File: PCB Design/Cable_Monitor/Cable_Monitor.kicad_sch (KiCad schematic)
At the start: 13 parts, among them P1 ${SIM.PARAMS}, P2 ${SIM.PARAMS}

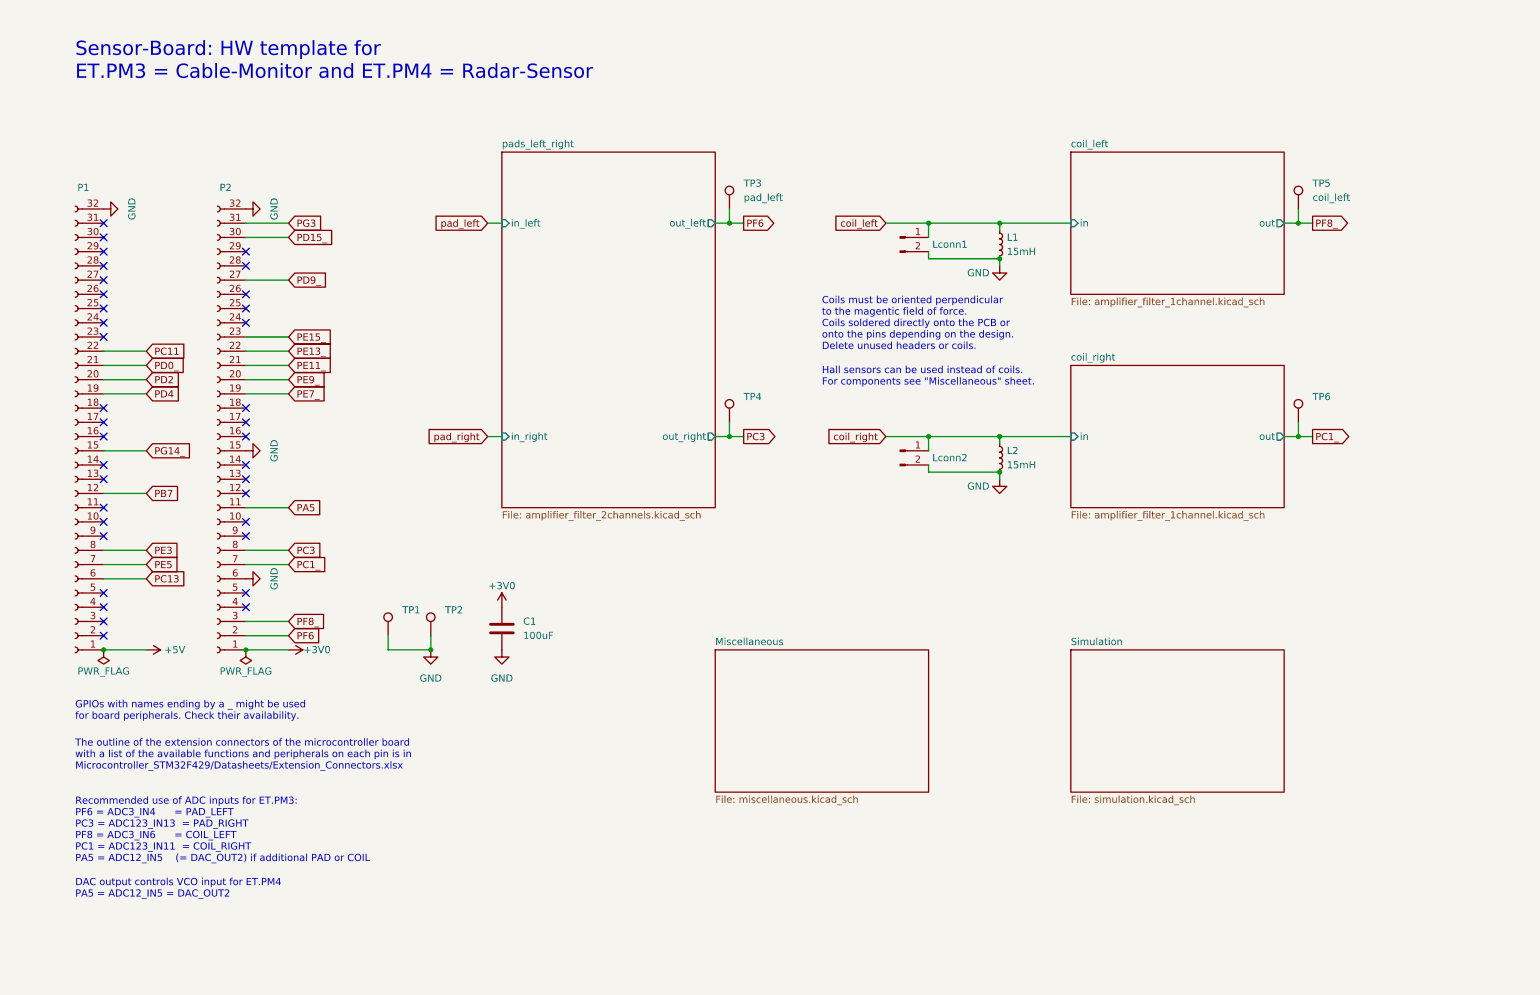
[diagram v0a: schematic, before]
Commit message: Modified Schematics
Added Virtual GND and adapted the Pads Left and Right
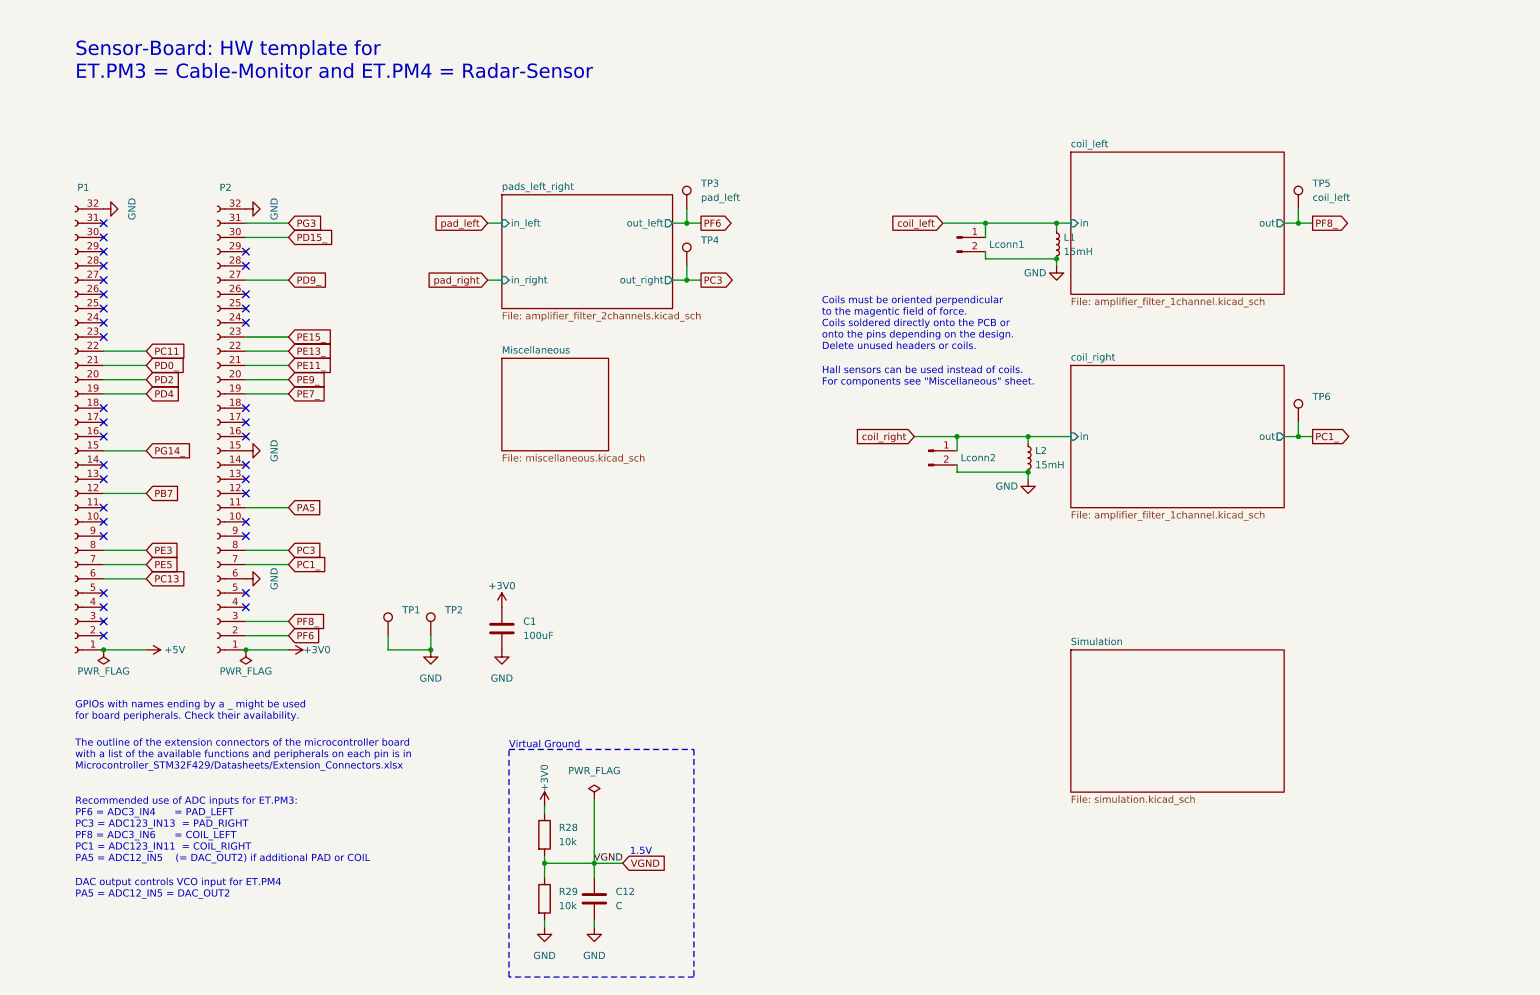
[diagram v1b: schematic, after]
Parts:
- added C12: C, symbol Device:C
- added R28, R29: 10k, symbol Device:R
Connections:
- net +3V0: now also R28.1
- net GND: now also C12.2, R29.2
- new net VGND: C12.1, R28.2, R29.1
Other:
- note added: "1.5V"
- note added: "Virtual Ground"
- moved on the sheet: L1, L2, Lconn1, Lconn2, TP3, TP4

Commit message: PCB Layout Update
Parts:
- added C4: 4.7uF, Capacitor_SMD:C_1206_3216Metric_Pad1.33x1.80mm_HandSolder, symbol Device:C
- added C4: C, symbol Device:C
- added C6: 100nF, Capacitor_SMD:C_0805_2012Metric_Pad1.18x1.45mm_HandSolder, symbol Device:C
- added C7: 10uF, Capacitor_SMD:C_0805_2012Metric_Pad1.18x1.45mm_HandSolder, symbol Device:C
- added J1: USB_B_Micro, symbol Connector:USB_B_Micro
- added TP3: Virtual Ground TP, symbol Connector:TestPoint
- added U3: SiP32508, Package_TO_SOT_SMD:TSOT-23-6_HandSoldering, symbol HW_template:SiP32508
- added U4: LD1117S33TR, Package_TO_SOT_SMD:SOT-223-3_TabPin2, symbol Regulator_Linear:LD1117S33TR_SOT223
- renumbered C12 to C2, L2 to L1, L1 to L2, Lconn2 to Lconn1, Lconn1 to Lconn2, R28 to R1, R29 to R2, TP3 to TP4, TP4 to TP5, TP5 to TP6, TP6 to TP7
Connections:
- net +3V0: now also C7.1, U4.2 (VO)
- net +5V: now also C4.1, C4.1, J1.1 (VBUS), U3.5 (IN), U3.6 (IN)
- net GND: now also C4.2, C4.2, C6.2, C7.2, J1.5 (GND), J1.6 (Shield), U3.4 (GND), U4.1 (GND)
- net VGND: now also TP3.1
- new net: C6.1, U3.1 (OUT), U3.2 (OUT), U4.3 (VI)
- new net Enable: U3.3 (EN)
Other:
- note added: "C4, C6 & C7 Values from Datasheet"
- note added: "Linear 3.3V low drop regulator"
- note added: "Load switch Can be used to power on with pushbutton and power off via microcontroller."
- note added: "Micro USB Connector for 5V external supply (Powerbank)"
- company: hhrt@zhaw.ch -> ZHAW
- title: Sensor-Board: HW template for ET.PM3 and ET.PM4 -> Cable Monitor
- moved on the sheet: C1, C2, R1, R2, TP1, TP2

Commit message: PCB Design Update
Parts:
- removed L1, L2: 15mH, Inductor_SMD:L_Bourns_SRN6045TA, symbol Device:L_Small
- removed Lconn1: Conn_01x02_Male, Connector_PinHeader_2.54mm:PinHeader_1x02_P2.54mm_Vertical, symbol Connector:Conn_01x02_Pin
- added BZ1: Buzzer, Buzzer_Beeper:Buzzer_12x9.5RM7.6, symbol Device:Buzzer
- added C? (x2): 100nF, Capacitor_SMD:C_0805_2012Metric_Pad1.18x1.45mm_HandSolder, symbol Device:C
- added LED1 (x2): LEDred_3mm, LED_THT:LED_D3.0mm, symbol Device:LED
- added Lconn2: Conn_01x02_Male, Connector_PinHeader_2.54mm:PinHeader_1x02_P2.54mm_Vertical, symbol Connector:Conn_01x02_Pin
- added Q1: BSS316N, Package_TO_SOT_SMD:SOT-23, symbol Transistor_FET:BSS138
- added R21 (x2): 62, Resistor_SMD:R_0805_2012Metric_Pad1.20x1.40mm_HandSolder, symbol Device:R
- added R26: 100k, Resistor_SMD:R_0805_2012Metric_Pad1.20x1.40mm_HandSolder, symbol Device:R
- added SW1: ${SIM.PARAMS}, Button_Switch_SMD:SW_SPST_PTS645, symbol Switch:SW_Push
- added U? (x2): DRV5053_THT, HW_template:TO-92Flat_wide, symbol Sensor_Magnetic:DRV5055A1xLPGxQ1
- C2: value C -> 1nF
- TP6: value coil_left -> HS_left
- TP7: value ${SIM.PARAMS} -> HS_right
- renumbered C4 to C?, C7 to C?, C6 to C?, Lconn2 to Lconn1, U4 to U?, U3 to U?
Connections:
- net +3V0: now also C?.2, C?.2, U?.1 (VCC), U?.1 (VCC)
- net +5V: now also BZ1.1 (-)
- net GND: now also C?.1, C?.1, LED1.1 (K), LED1.1 (K), Lconn2.2 (Pin_2), Q1.2 (S), R26.2, U?.2 (GND), U?.2 (GND)
- net PA5: now also Q1.1 (G), R26.1
- net coil_left renamed HS_left
- net HS_left: now also U?.3 (OUT)
- new net: BZ1.2 (+), Q1.3 (D)
- new net: LED1.2 (A), R21.2 (x2)
- new net HS_right: Lconn2.1 (Pin_1), U?.3 (OUT)
- new net LED_LEFT_EN: R21.1
- new net LED_RIGHT_EN: R21.1
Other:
- sheet coil_left renamed hall-sensor_left_right
- removed sheet Simulation
- removed sheet coil_right
- sheet hall-sensor_left_right ports: added in_left, in_right, out_left, out_right; removed in, out
- note added: "PWM controlled Buzzer"
- note removed: "Coils must be oriented perpendicular to the magentic field of force. Coils soldered directly onto the PCB or onto the pins depending on the design. Delete unused headers or coils."
- note removed: "Hall sensors can be used instead of coils. For components see "Miscellaneous" sheet."
- moved on the sheet: TP6, TP7

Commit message: Letzte Anpassungen am Schema
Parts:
- added TP14: PWM_Buzzer, TestPoint:TestPoint_Loop_D2.60mm_Drill1.6mm_Beaded, symbol Connector:TestPoint
- added TP3, TP4: pad_left_in, TestPoint:TestPoint_Loop_D2.60mm_Drill1.6mm_Beaded, symbol Connector:TestPoint
- added TP8: HS_left_in, TestPoint:TestPoint_Loop_D2.60mm_Drill1.6mm_Beaded, symbol Connector:TestPoint
- added TP9: HS_right_in, TestPoint:TestPoint_Loop_D2.60mm_Drill1.6mm_Beaded, symbol Connector:TestPoint
- C4: value C -> 100uF
- TP10: renamed from TP6; value HS_left -> HS_left_out
- TP11: renamed from TP7; value HS_right -> HS_right_out
- TP6: renamed from TP4; value pad_left -> pad_left_out
- TP7: renamed from TP5; value ${SIM.PARAMS} -> pad_right_out
- gave numbers to parts that had none: 9
- renumbered TP3 to TP5
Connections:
- net LED_LEFT_EN is gone; now on net PE15_: R21.1
- net LED_RIGHT_EN is gone; now on net PE13_: R21.1
- net PA5: now also TP14.1
- net pad_left: now also TP3.1
- net pad_right: now also TP4.1
- net HS_left renamed hall-sensor_left_right/in_left
- net hall-sensor_left_right/in_left: now also TP8.1
- net HS_right renamed hall-sensor_left_right/in_right
- net hall-sensor_left_right/in_right: now also TP9.1
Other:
- removed sheet Miscellaneous
- note added: "Cable-Monitor A Project by A.Horvat and T.Wey for PM3 Module ZHAW"
- note added: "Left and Right LED's to show direction of Fields"
- note added: "Pads for picking up Electrical Field. Including Filtering and amplifying"
- note removed: "Sensor-Board: HW template for ET.PM3 = Cable-Monitor and ET.PM4 = Radar-Sensor"
- moved on the sheet: BZ1, C1, LED1, Q1, R21, R26, TP6, TP7

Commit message: Schema Updates, bald Fertig
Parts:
- added TP11: 5V, TestPoint:TestPoint_Loop_D2.60mm_Drill1.6mm_Beaded, symbol Connector:TestPoint
- added TP14: 3V, TestPoint:TestPoint_Loop_D2.60mm_Drill1.6mm_Beaded, symbol Connector:TestPoint
- added TP3, TP4, TP5, TP6: GND, TestPoint:TestPoint_Loop_D2.60mm_Drill1.6mm_Beaded, symbol Connector:TestPoint
- C2, C4: footprint (none) -> Capacitor_SMD:C_0805_2012Metric_Pad1.18x1.45mm_HandSolder
- J1: footprint (none) -> Connector_USB:USB_Micro-B_Molex-105017-0001
- R1, R2: footprint (none) -> Resistor_SMD:R_0805_2012Metric_Pad1.20x1.40mm_HandSolder
- TP1, TP2: value ${SIM.PARAMS} -> GND
- TP8: renamed from TP5; footprint (none) -> TestPoint:TestPoint_Loop_D2.60mm_Drill1.6mm_Beaded
- renumbered LED1 to LED2, R26 to R3, R21 to R4, R21 to R5, TP4 to TP10, TP6 to TP12, TP7 to TP13, TP8 to TP15, TP9 to TP16, TP10 to TP17, TP11 to TP18, TP14 to TP7, TP3 to TP9
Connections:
- net +3V0: now also TP14.1
- net +5V: now also TP11.1
- net GND: now also TP3.1, TP4.1, TP5.1, TP6.1; no longer J1.6 (Shield)
- no-connect marks 36 -> 40
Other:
- note added: "Hall-Sensor to detect Magnetic Fields (and allow us to calculate Current) includes filtering and amplifying"
- moved on the sheet: C1, C7, C8, LED1, LED2, R4, R5, TP13, TP15, TP16, TP17, TP18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

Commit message: Update
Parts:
- added D1, D2: SS13L_R3G, SODFL3618X143N, symbol SS13L_R3G:SS13L_R3G
- added R4: 10k, Resistor_SMD:R_0805_2012Metric_Pad1.20x1.40mm_HandSolder, symbol Device:R
- added R5: 30k, Resistor_SMD:R_0805_2012Metric_Pad1.20x1.40mm_HandSolder, symbol Device:R
- added R6: 43k, Resistor_SMD:R_0805_2012Metric_Pad1.20x1.40mm_HandSolder, symbol Device:R
- SW1: value ${SIM.PARAMS} -> On / Off Button
- TP7: renamed from TP8; value Virtual Ground TP -> VGND
- renumbered Lconn1 to HS_Left1, Lconn2 to HS_right1, R4 to R7, R5 to R8, TP7 to TP8
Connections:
- net +5V: now also SW1.2
- net Enable: now also D1.1 (K), D2.1 (K), R4.2
- net GND: now also R4.1, R6.1
- net PE3: now also R5.2, R6.2
- net PE5: now also D1.2 (A)
- net at SW1.1: now also D2.2 (A), R5.1
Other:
- note added: "Logic for On/Off Switch (soft latching power circuit)"
- note added: "This voltage divider converts the 5V Power source to 3V (Board I/O). This allows us to read the switch"
- moved on the sheet: BZ1, C1, C2, C3, C4, C5, C6, J1, LED1, LED2, P1, P2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

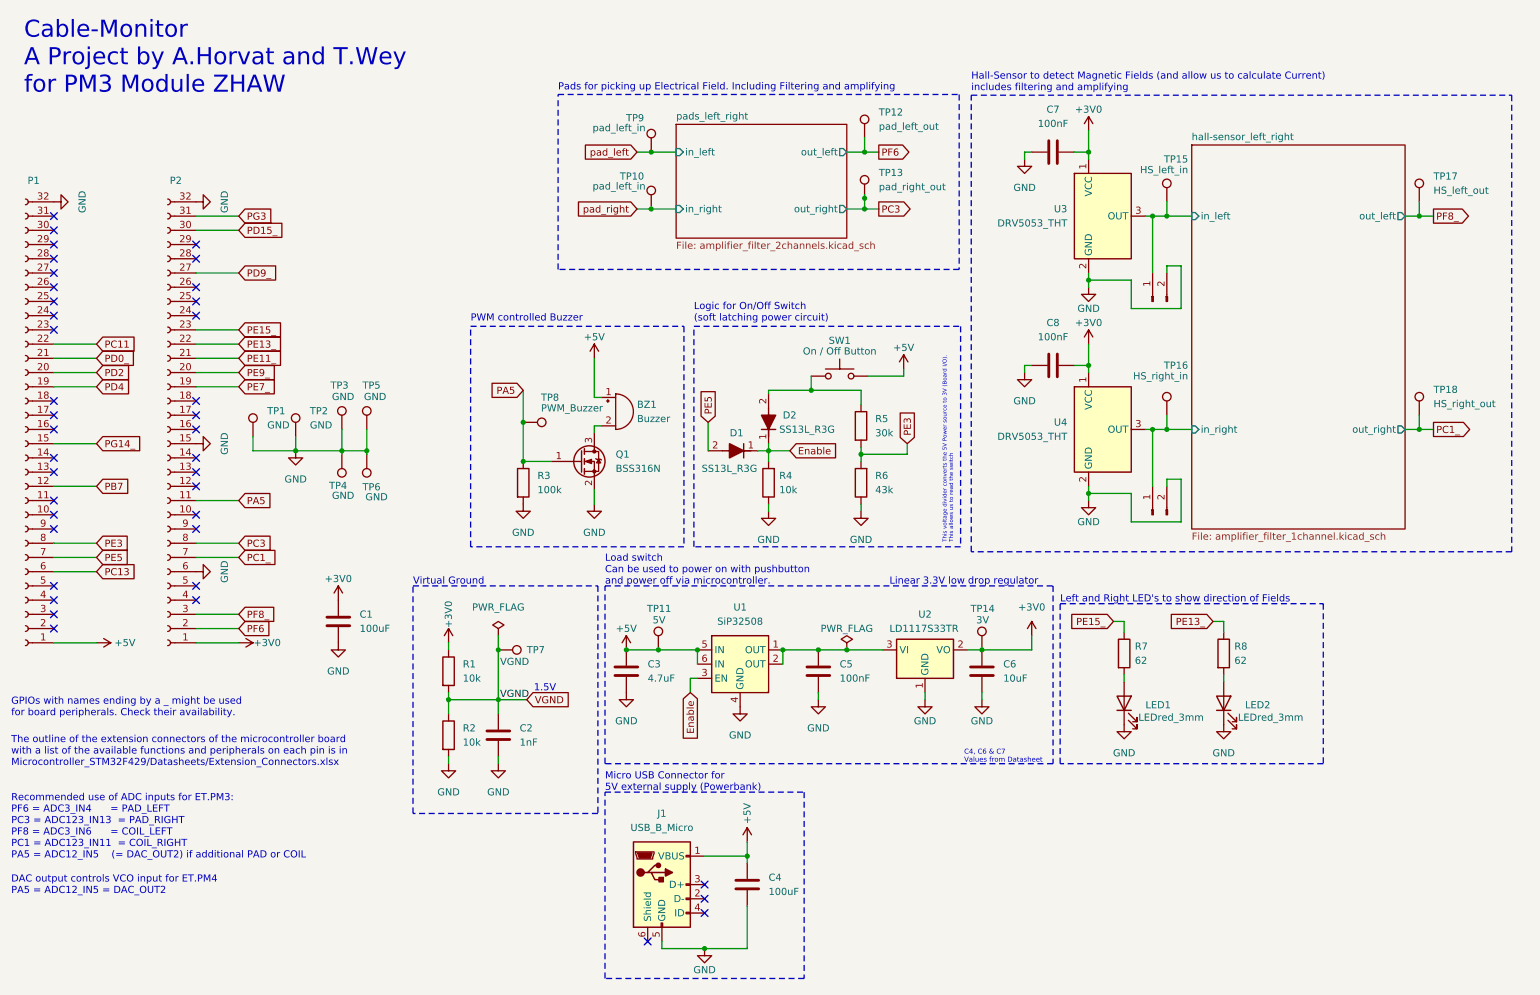
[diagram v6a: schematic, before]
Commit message: Schema PDF Export
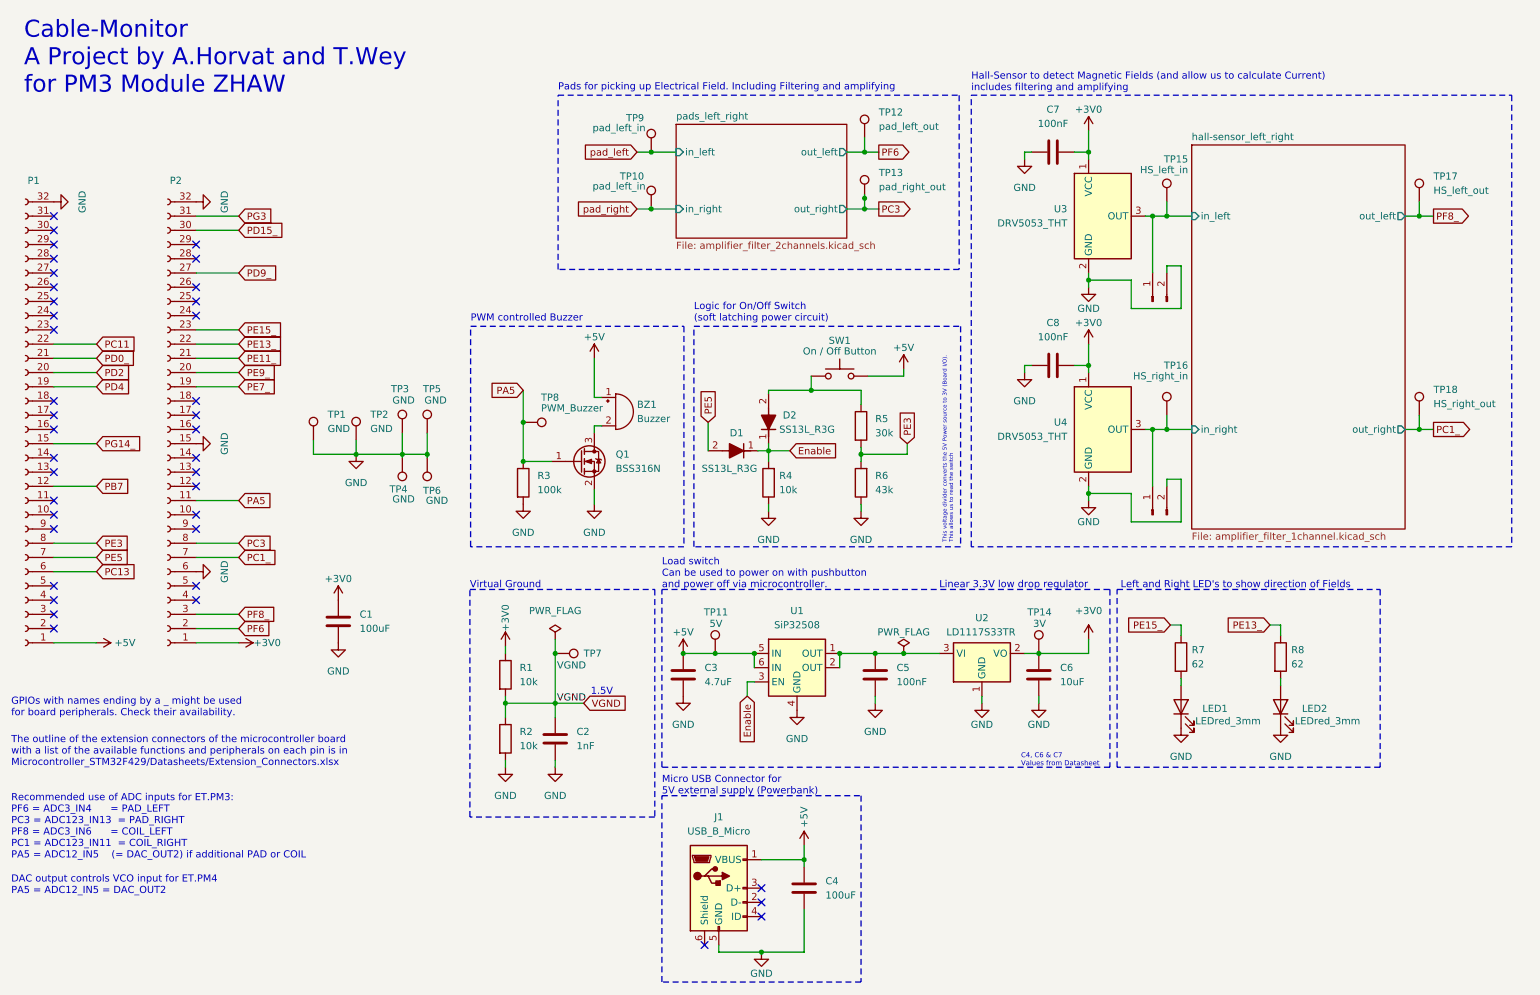
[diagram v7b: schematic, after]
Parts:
- C4: footprint Capacitor_SMD:C_0805_2012Metric_Pad1.18x1.45mm_HandSolder -> Capacitor_SMD:C_1206_3216Metric_Pad1.33x1.80mm_HandSolder
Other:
- moved on the sheet: C2, C3, C4, C5, C6, J1, LED1, LED2, R1, R2, R7, R8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

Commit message: Almost Donezo
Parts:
- TP10: value pad_left_in -> pad_right_in
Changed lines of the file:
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@@
       (effects (font (size 1.27 1.27)) (justify right))
     )
-    (property "Value" "pad_left_in" (at 127.254 44.196 0)
+    (property "Value" "pad_right_in" (at 127.254 44.196 0)
       (effects (font (size 1.27 1.27)) (justify right))
     )
